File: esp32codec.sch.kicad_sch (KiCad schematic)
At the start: 7 parts, among them U13 TL072, U4 NAU88C22YG

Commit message: powersupply added
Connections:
- net GND: now also U4.18 (MODE)
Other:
- added sheet power (esp32power.sch.kicad_sch)
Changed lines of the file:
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@@
+	(wire
+		(pts
+			(xy 88.9 82.55) (xy 93.98 82.55)
+		)
+		(stroke
+			(width 0)
+			(type default)
+		)
+	)
 	(wire
 		(pts
@@
 	(symbol
 		(lib_id "power:GND")
+		(at 88.9 82.55 0)
+		(unit 1)
+		(exclude_from_sim no)
+		(in_bom yes)
+		(on_board yes)
+		(dnp no)
+		(fields_autoplaced yes)
+		(property "Reference" "#PWR83"
+			(at 88.9 88.9 0)
+			(effects
+				(font
+					(size 1.27 1.27)
+				)
+				(hide yes)
+			)
+		)
+		(property "Value" "GND"
+			(at 88.9 87.63 0)
+			(effects
+				(font
+					(size 1.27 1.27)
+				)
+			)
+		)
+		(property "Footprint" ""
+			(at 88.9 82.55 0)
+			(effects
+				(font
+					(size 1.27 1.27)
+				)
+				(hide yes)
+			)
+		)
+		(property "Datasheet" ""
+			(at 88.9 82.55 0)
+			(effects
+				(font
+					(size 1.27 1.27)
+				)
+				(hide yes)
+			)
+		)
+		(property "Description" "Power symbol creates a global label with name \"GND\" , ground"
+			(at 88.9 82.55 0)
+			(effects
+				(font
+					(size 1.27 1.27)
+				)
+				(hide yes)
+			)
+		)
+		(pin "1"
+		)
+		(instances
+			(project ""
+				(path "/c4754426-a41b-4341-9d09-2e389619f3d6/32d637b3-b81c-4082-b7fa-739e0cc157fd"
+					(reference "#PWR83")
+					(unit 1)
+				)
+			)
+		)
+	)
+	(symbol
+		(lib_id "power:GND")
 		(at 146.05 81.28 0)
 		(unit 1)
@@
 				)
 			)
+		)
+	)
+	(sheet
+		(at 162.56 132.08)
+		(size 12.7 10.16)
+		(fields_autoplaced yes)
+		(stroke
+			(width 0.1524)
+			(type solid)
+		)
+		(fill
+			(color 0 0 0 0.0000)
+		)
+		(property "Sheetname" "power"
+			(at 162.56 131.3684 0)
+			(effects
+				(font
+					(size 1.27 1.27)
+				)
+				(justify left bottom)
+			)
+		)
+		(property "Sheetfile" "esp32power.sch.kicad_sch"
+			(at 162.56 142.8246 0)
+			(effects
+				(font
+					(size 1.27 1.27)
+				)
+				(justify left top)
+			)
+		)
+		(instances
+			(project "esp32"
+				(path "/c4754426-a41b-4341-9d09-2e389619f3d6/32d637b3-b81c-4082-b7fa-739e0cc157fd"
+					(page "9")
+				)
+			)

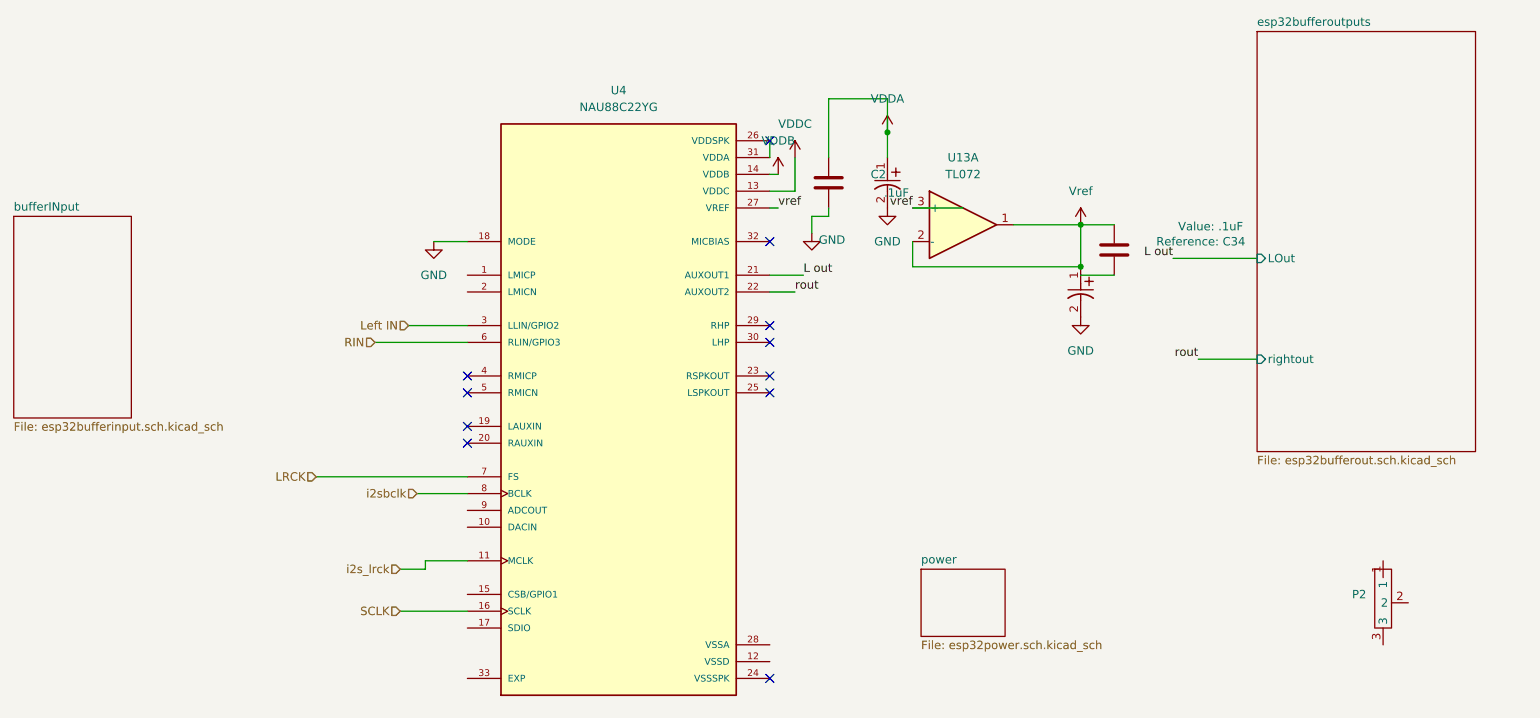
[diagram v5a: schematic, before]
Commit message: UPDATED AU88 CODEC PINS
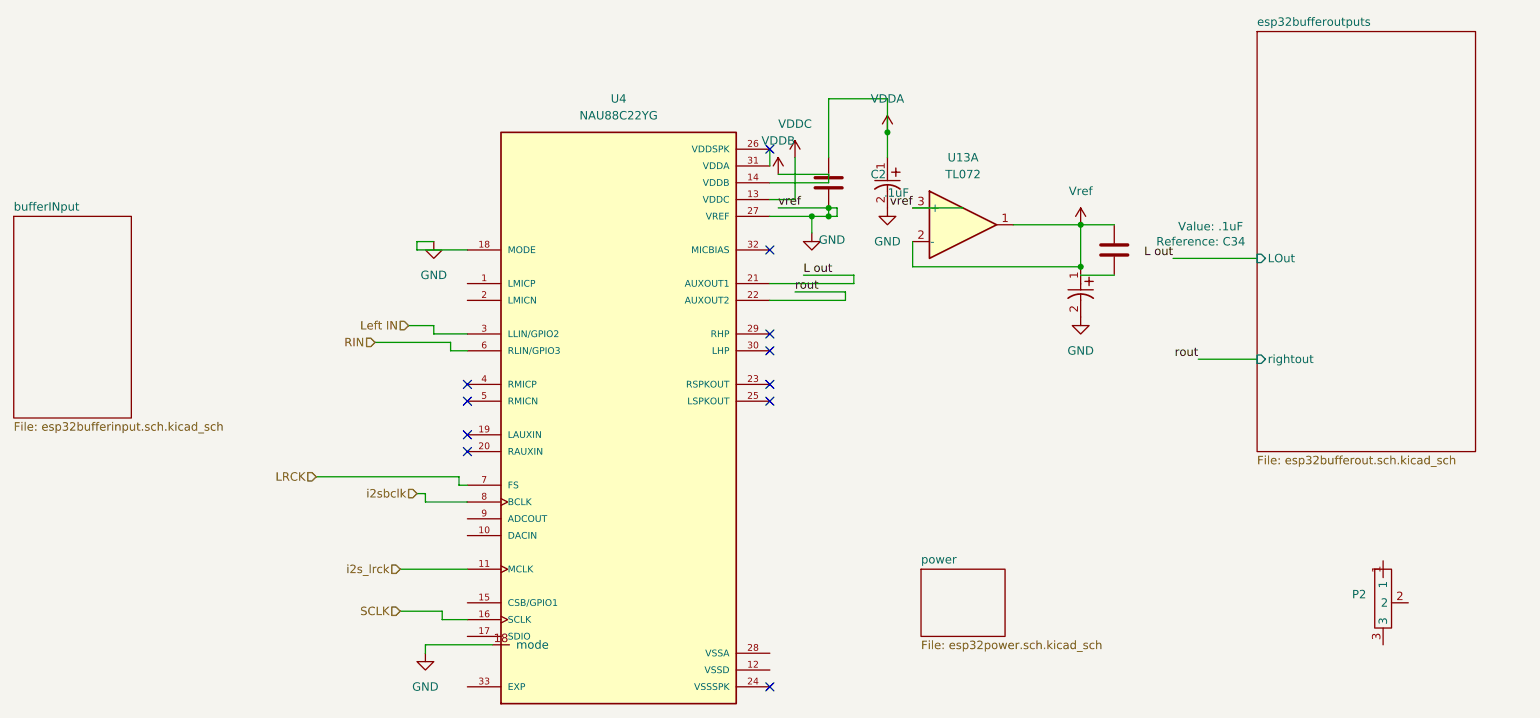
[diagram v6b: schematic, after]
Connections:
- net vref is gone; now on net GND: U13.3 (+), U4.27 (VREF)

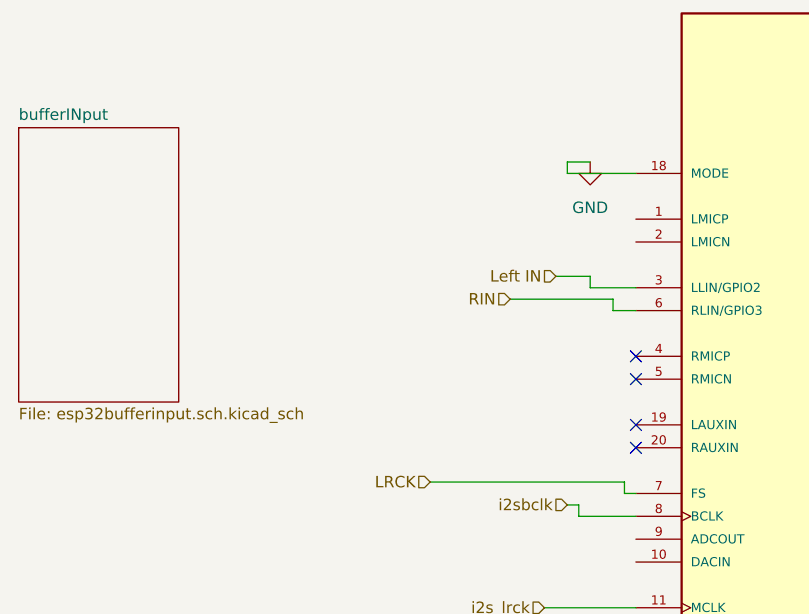
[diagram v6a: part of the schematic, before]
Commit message: added codec buffers
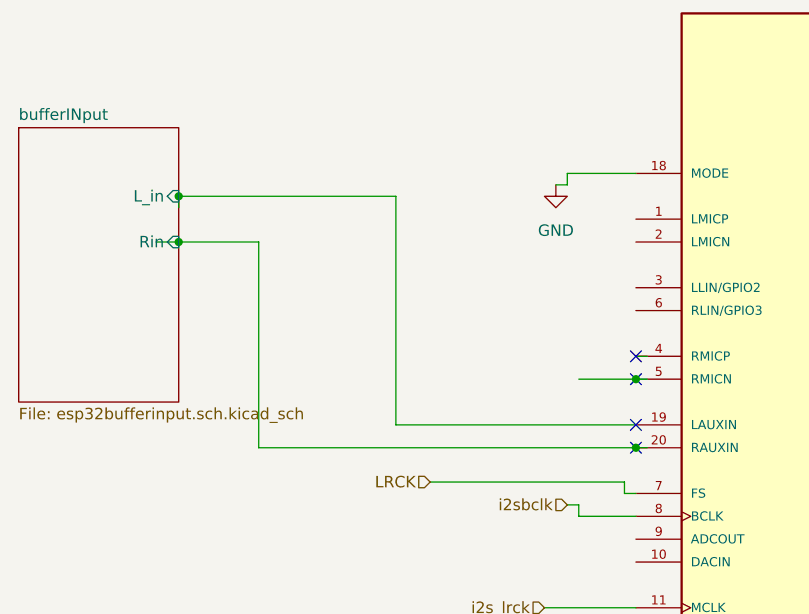
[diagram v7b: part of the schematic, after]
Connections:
- net bufferINput/L_in: now reaches U4.19 (LAUXIN)
- net bufferINput/Rin: now reaches U4.20 (RAUXIN)
- net Left IN: no longer names the net of U4.3 (LLIN/GPIO2)
- net RIN: no longer names the net of U4.6 (RLIN/GPIO3)
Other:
- sheet bufferINput ports: added L_in, Rin; removed none
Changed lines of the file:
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@@
 	(paper "A4")
+	(junction
+		(at 43.18 91.44)
+		(diameter 0)
+		(color 0 0 0 0)
+	)
 	(junction
 		(at 186.69 86.36)
@@
 	)
 	(junction
+		(at 43.18 86.36)
+		(diameter 0)
+		(color 0 0 0 0)
+	)
+	(junction
 		(at 157.48 66.04)
+		(diameter 0)
+		(color 0 0 0 0)
+	)
+	(junction
+		(at 93.98 106.68)
+		(diameter 0)
+		(color 0 0 0 0)
+	)
+	(junction
+		(at 93.98 114.3)
 		(diameter 0)
 		(color 0 0 0 0)
@@
 	(wire
 		(pts
+			(xy 67.31 111.76) (xy 67.31 86.36)
+		)
+		(stroke
+			(width 0)
+			(type default)
+		)
+	)
+	(wire
+		(pts
 			(xy 87.63 121.92) (xy 87.63 120.65)
 		)
@@
 	(wire
 		(pts
-			(xy 88.9 95.25) (xy 85.09 95.25)
-		)
-		(stroke
-			(width 0)
-			(type default)
-		)
-	)
-	(wire
-		(pts
-			(xy 91.44 97.79) (xy 80.01 97.79)
-		)
-		(stroke
-			(width 0)
-			(type default)
-		)
-	)
-	(wire
-		(pts
 			(xy 151.13 91.44) (xy 139.7 91.44)
 		)
@@
 	(wire
 		(pts
+			(xy 95.25 114.3) (xy 93.98 114.3)
+		)
+		(stroke
+			(width 0)
+			(type default)
+		)
+	)
+	(wire
+		(pts
+			(xy 93.98 106.68) (xy 95.25 106.68)
+		)
+		(stroke
+			(width 0)
+			(type default)
+		)
+	)
+	(wire
+		(pts
 			(xy 149.86 78.74) (xy 148.59 78.74)
 		)
@@
 	(wire
 		(pts
+			(xy 52.07 114.3) (xy 52.07 91.44)
+		)
+		(stroke
+			(width 0)
+			(type default)
+		)
+	)
+	(wire
+		(pts
 			(xy 148.59 77.47) (xy 140.97 77.47)
 		)
@@
 	(wire
 		(pts
+			(xy 43.18 91.44) (xy 52.07 91.44)
+		)
+		(stroke
+			(width 0)
+			(type default)
+		)
+	)
+	(wire
+		(pts
 			(xy 186.69 87.63) (xy 191.77 87.63)
 		)
@@
 	(wire
 		(pts
-			(xy 91.44 99.06) (xy 91.44 97.79)
+			(xy 43.18 87.63) (xy 43.18 86.36)
+		)
+		(stroke
+			(width 0)
+			(type default)
+		)
+	)
+	(wire
+		(pts
+			(xy 87.63 106.68) (xy 93.98 106.68)
 		)
 		(stroke
@@
 	(wire
 		(pts
-			(xy 88.9 96.52) (xy 88.9 95.25)
-		)
-		(stroke
-			(width 0)
-			(type default)
-		)
-	)
-	(wire
-		(pts
 			(xy 87.63 143.51) (xy 97.79 143.51)
 		)
@@
 	(wire
 		(pts
-			(xy 88.9 96.52) (xy 93.98 96.52)
-		)
-		(stroke
-			(width 0)
-			(type default)
-		)
-	)
-	(wire
-		(pts
 			(xy 87.63 120.65) (xy 86.36 120.65)
 		)
@@
 	(wire
 		(pts
+			(xy 95.25 104.14) (xy 93.98 104.14)
+		)
+		(stroke
+			(width 0)
+			(type default)
+		)
+	)
+	(wire
+		(pts
 			(xy 151.13 90.17) (xy 143.51 90.17)
 		)
@@
 	(wire
 		(pts
-			(xy 86.36 82.55) (xy 88.9 82.55)
+			(xy 93.98 114.3) (xy 52.07 114.3)
+		)
+		(stroke
+			(width 0)
+			(type default)
+		)
+	)
+	(wire
+		(pts
+			(xy 86.36 85.09) (xy 85.09 85.09)
 		)
 		(stroke
@@
 	(wire
 		(pts
-			(xy 91.44 99.06) (xy 93.98 99.06)
+			(xy 93.98 111.76) (xy 67.31 111.76)
+		)
+		(stroke
+			(width 0)
+			(type default)
+		)
+	)
+	(wire
+		(pts
+			(xy 40.64 91.44) (xy 43.18 91.44)
 		)
 		(stroke
@@
 	(wire
 		(pts
-			(xy 86.36 83.82) (xy 86.36 82.55)
+			(xy 86.36 85.09) (xy 86.36 83.82)
+		)
+		(stroke
+			(width 0)
+			(type default)
+		)
+	)
+	(wire
+		(pts
+			(xy 43.18 86.36) (xy 67.31 86.36)
 		)
 		(stroke
@@
 			)
 			(justify right bottom)
-		)
-	)
-	(hierarchical_label "RIN"
-		(shape input)
-		(at 80.01 97.79 180)
-		(effects
-			(font
-				(size 1.27 1.27)
-			)
-			(justify right)
 		)
 	)
@@
 		(shape input)
 		(at 86.36 120.65 180)
-		(effects
-			(font
-				(size 1.27 1.27)
-			)
-			(justify right)
-		)
-	)
-	(hierarchical_label "Left IN"
-		(shape input)
-		(at 85.09 95.25 180)
 		(effects
 			(font
@@
 	(symbol
 		(lib_id "power:GND")
-		(at 88.9 82.55 0)
+		(at 85.09 85.09 0)
 		(unit 1)
 		(exclude_from_sim no)
@@
 		(fields_autoplaced yes)
 		(property "Reference" "#PWR83"
-			(at 88.9 88.9 0)
+			(at 85.09 91.44 0)
 			(effects
 				(font
@@
 		)
 		(property "Value" "GND"
-			(at 88.9 87.63 0)
+			(at 85.09 90.17 0)
 			(effects
 				(font
@@
 		)
 		(property "Footprint" ""
-			(at 88.9 82.55 0)
+			(at 85.09 85.09 0)
 			(effects
 				(font
@@
 		)
 		(property "Datasheet" ""
-			(at 88.9 82.55 0)
+			(at 85.09 85.09 0)
 			(effects
 				(font
@@
 		)
 		(property "Description" "Power symbol creates a global label with name \"GND\" , ground"
-			(at 88.9 82.55 0)
+			(at 85.09 85.09 0)
 			(effects
 				(font
@@
 			)
 		)
+		(pin "Rin" input
+			(at 43.18 91.44 0)
+			(effects
+				(font
+					(size 1.27 1.27)
+				)
+				(justify right)
+			)
+		)
+		(pin "L_in" input
+			(at 43.18 86.36 0)
+			(effects
+				(font
+					(size 1.27 1.27)
+				)
+				(justify right)
+			)
+		)
